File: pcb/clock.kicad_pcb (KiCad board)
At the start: 2 copper layers, 34.8 x 24 mm, 11 parts, among them J1 Conn_01x03_Pin, J2 Conn_01x03_Pin, J3 Conn_01x03_Pin, J4 Conn_01x03_Pin, U1 ESP32-C3-SuperMini

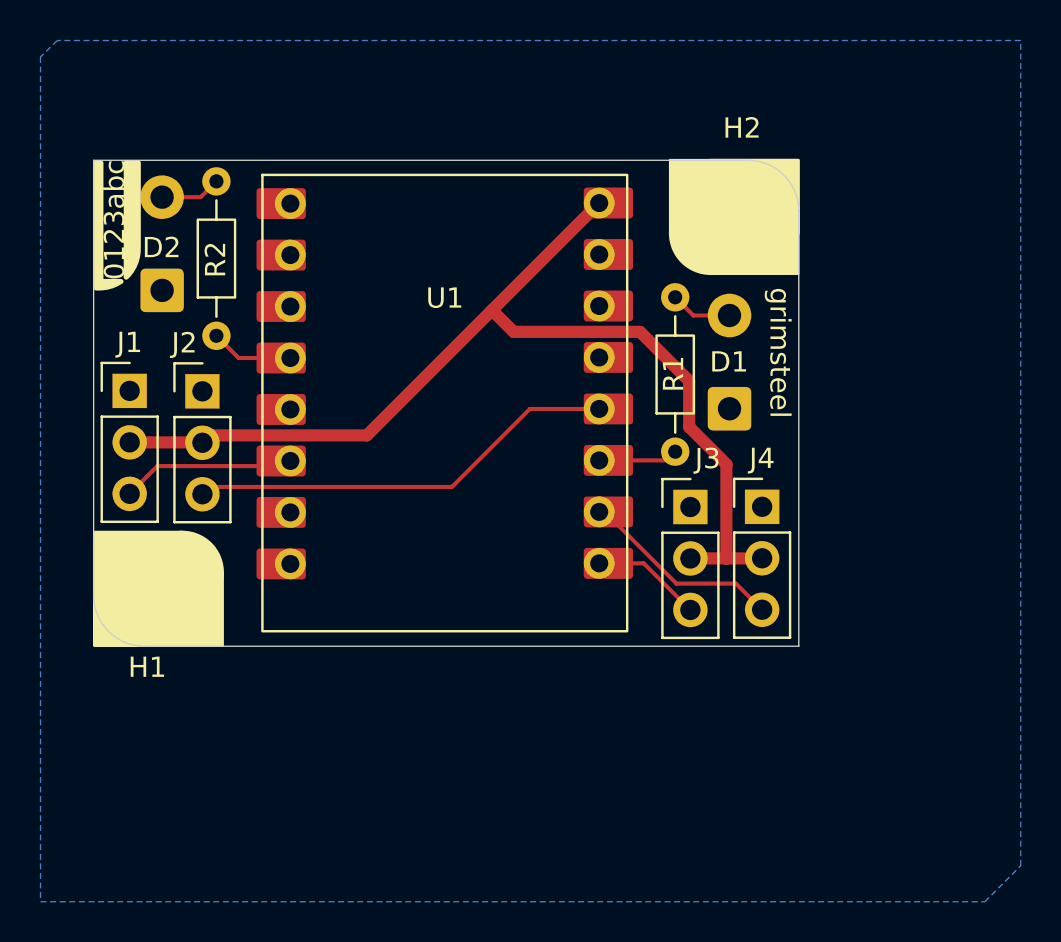
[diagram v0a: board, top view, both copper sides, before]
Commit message: pcb: led improvements
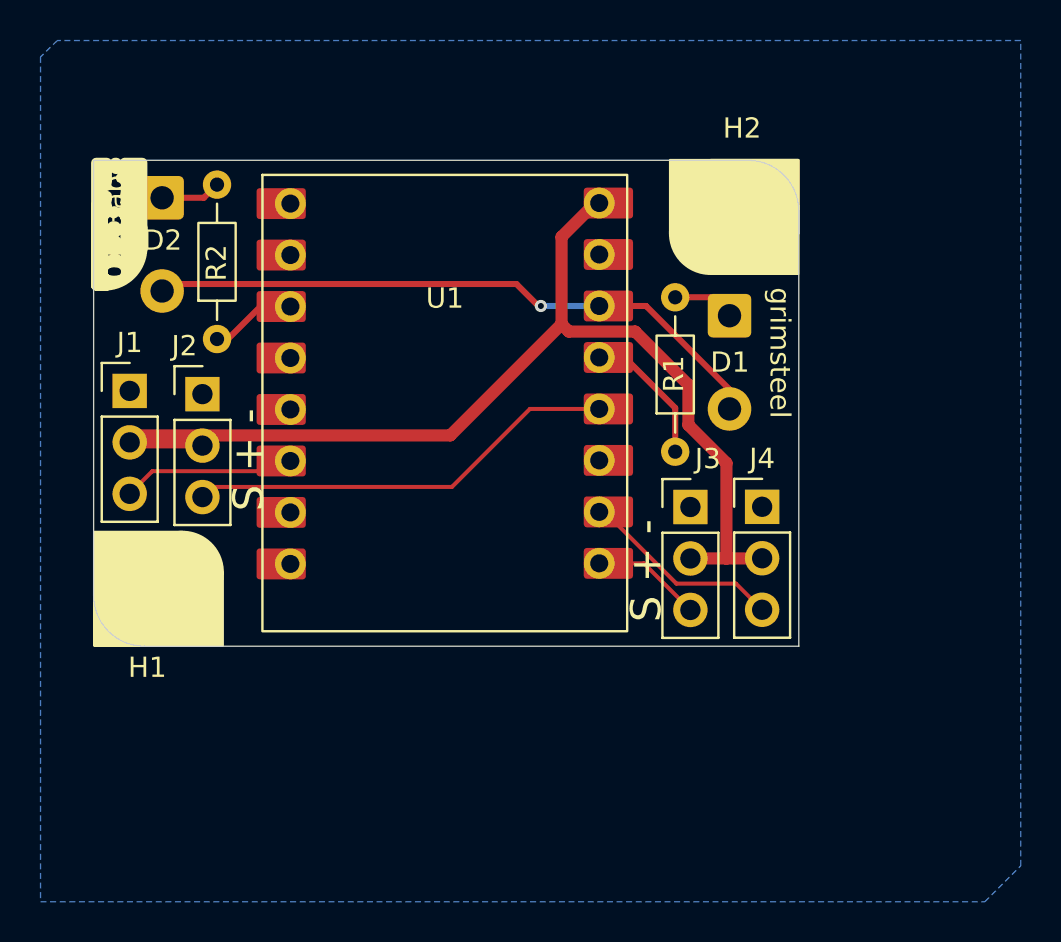
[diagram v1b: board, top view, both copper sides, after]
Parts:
- moved D1 4.59 mm to (56.0, 48.4), turned to -90 degrees
- moved D2 4.57 mm to (28.0, 42.6), turned to -90 degrees
- moved R2 0.16 mm to (30.7, 49.6)
- moved J2 0.14 mm to (30.0, 52.3)
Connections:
- D1 pad 1: GND -> Net-(D1-K)
- D1 pad 2: Net-(D1-A) -> +3.3V
- D2 pad 1: GND -> Net-(D2-K)
- D2 pad 2: Net-(D2-A) -> +3.3V
- R1 pad 2: Net-(D1-A) -> Net-(D1-K)
- R2 pad 2: Net-(D2-A) -> Net-(D2-K)
- U1 pad 11: unconnected-(U1-GPIO7-Pad11) -> LED_2
- U1 pad 12: LED_2 -> unconnected-(U1-GPIO8-Pad12)_1
- U1 pad 3: LED_1 -> unconnected-(U1-GPIO2-Pad3)
- U1 pad 5: unconnected-(U1-GPIO4-Pad5)_1 -> LED_1
- U1 pad 6: unconnected-(U1-3V3-Pad6)_1 -> +3.3V
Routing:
- net +3.3V: track 0.00 -> 30.8 mm, vias 0 -> 1
- net Net-(D1-K): track 0.00 -> 3.06 mm
- net Net-(D1-A): track 3.05 -> 0.00 mm
- net LED_1: track 3.47 -> 6.49 mm
- net Net-(D2-A): track 3.00 -> 0.00 mm
- net Net-(D2-K): track 0.00 -> 2.98 mm
- net +5V: track 52.3 -> 54.6 mm
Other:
- board text added: "S + -"

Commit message: firmware: add esphome firmware
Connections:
- J2 pad 3: SERVO_3 -> SERVO_2
- J3 pad 3: SERVO_2 -> SERVO_3
- U1 pad 1: SERVO_2 -> SERVO_3
- U1 pad 4: SERVO_3 -> SERVO_2
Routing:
- net SERVO_3: track 21.3 -> 5.00 mm
- net SERVO_2: track 5.00 -> 21.3 mm
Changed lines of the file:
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@@
 			(layers "*.Cu" "*.Mask")
 			(remove_unused_layers no)
-			(net "SERVO_3")
+			(net "SERVO_2")
 			(pinfunction "Pin_3_3")
 			(pintype "passive")
@@
 			(layers "*.Cu" "*.Mask")
 			(remove_unused_layers no)
-			(net "SERVO_2")
+			(net "SERVO_3")
 			(pinfunction "Pin_3_3")
 			(pintype "passive")
@@
 			(layers "*.Cu" "*.Mask")
 			(remove_unused_layers no)
-			(net "SERVO_2")
+			(net "SERVO_3")
 			(pinfunction "GPIO0_1")
 			(pintype "bidirectional")
@@
 			(layers "F.Cu" "F.Mask")
 			(roundrect_rratio 0.1)
-			(net "SERVO_2")
+			(net "SERVO_3")
 			(pinfunction "GPIO0_1")
 			(pintype "bidirectional")
@@
 			(layers "*.Cu" "*.Mask")
 			(remove_unused_layers no)
-			(net "SERVO_3")
+			(net "SERVO_2")
 			(pinfunction "GPIO3_4")
 			(pintype "bidirectional")
@@
 			(layers "F.Cu" "F.Mask")
 			(roundrect_rratio 0.1)
-			(net "SERVO_3")
+			(net "SERVO_2")
 			(pinfunction "GPIO3_4")
 			(pintype "bidirectional")
@@
 	)
 	(segment
+		(start 50.004 60.66)
+		(end 51.75 60.66)
+		(width 0.2)
+		(layer "F.Cu")
+		(net "SERVO_3")
+	)
+	(segment
+		(start 51.75 60.66)
+		(end 54.05 62.96)
+		(width 0.2)
+		(layer "F.Cu")
+		(net "SERVO_3")
+	)
+	(segment
 		(start 42.28 56.89)
 		(end 46.13 53.04)
 		(width 0.2)
 		(layer "F.Cu")
-		(net "SERVO_3")
+		(net "SERVO_2")
 	)
 	(segment
@@
 		(width 0.2)
 		(layer "F.Cu")
-		(net "SERVO_3")
+		(net "SERVO_2")
 	)
 	(segment
@@
 		(width 0.2)
 		(layer "F.Cu")
-		(net "SERVO_3")
+		(net "SERVO_2")
 	)
 	(segment
@@
 		(width 0.2)
 		(layer "F.Cu")
-		(net "SERVO_3")
-	)
-	(segment
-		(start 50.004 60.66)
-		(end 51.75 60.66)
-		(width 0.2)
-		(layer "F.Cu")
-		(net "SERVO_2")
-	)
-	(segment
-		(start 51.75 60.66)
-		(end 54.05 62.96)
-		(width 0.2)
-		(layer "F.Cu")
